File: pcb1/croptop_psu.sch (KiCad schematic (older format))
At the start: 35 parts, among them J3 5V USB, U2 REG71055, U3 FAN5333BSX, U4 MIC23050, U5 TC1014

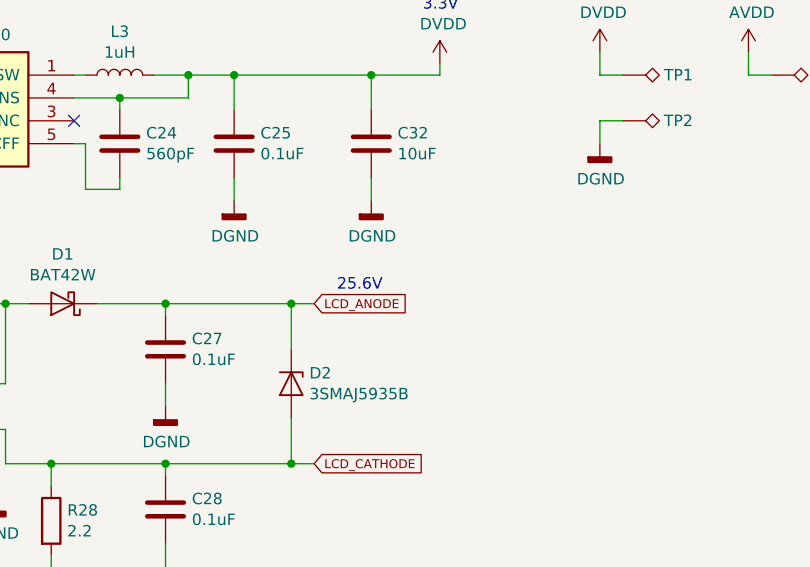
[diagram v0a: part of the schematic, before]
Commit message: Updated pin out
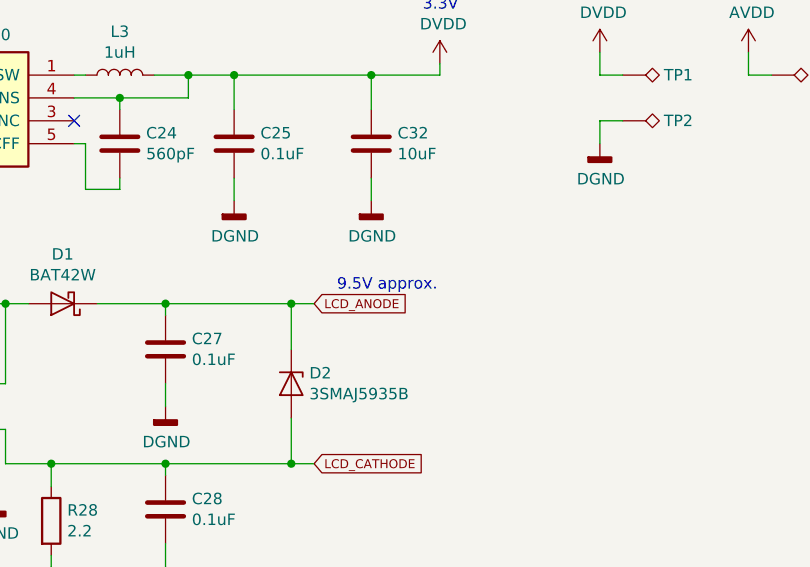
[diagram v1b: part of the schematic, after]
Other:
- note added: "9.5V approx.\n"
- note removed: "25.6V"
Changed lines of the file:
@@
 Connection ~ 4900 2700
 Text Notes 6650 4700 0    50   ~ 0
-25.6V
+9.5V approx.\n
 $Comp
 L Device:D_Zener D2
